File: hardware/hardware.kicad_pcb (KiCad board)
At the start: 2 copper layers, 110.5 x 66.5 mm, 23 parts, among them J1 DIN-5_180degree, U1 Teensy3.2, U2 TeensyAudioShield3.2, U3 6N138

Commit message: Change MIDI Out label to MIDI In
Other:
- board text added: "MIDI In"
- board text removed: "MIDI Out"

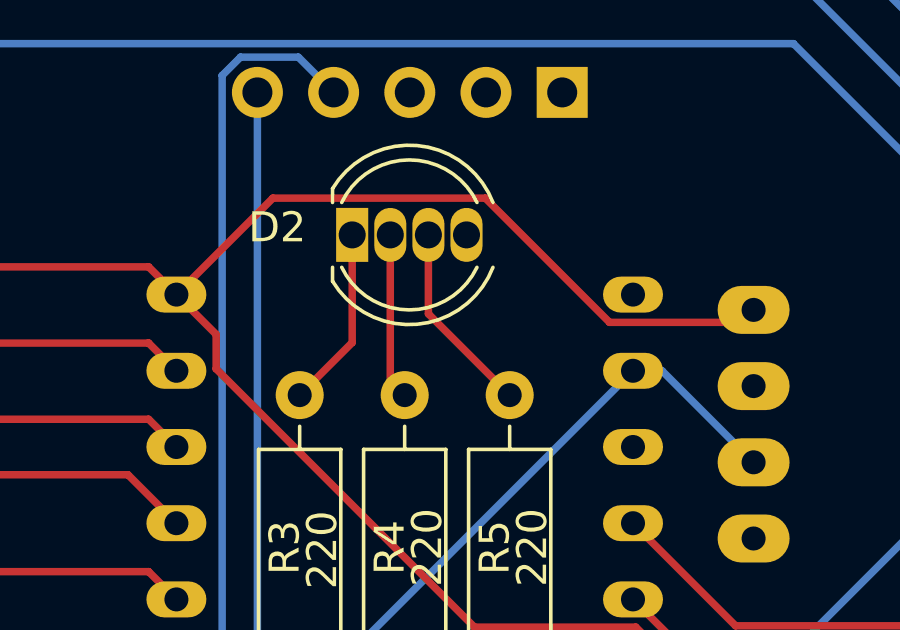
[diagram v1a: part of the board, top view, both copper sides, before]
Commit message: Make footprint match LED pinout even if schematic looks wrong
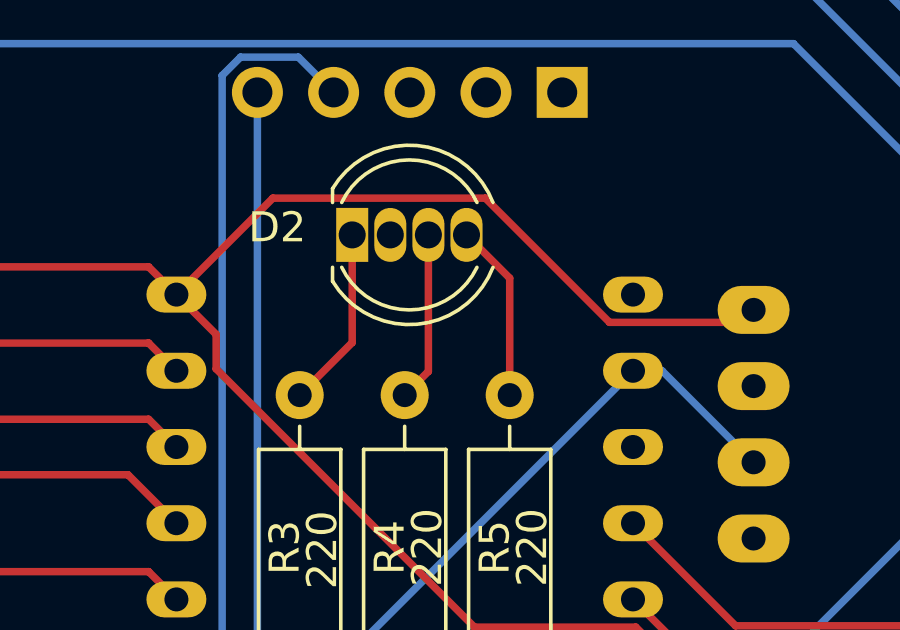
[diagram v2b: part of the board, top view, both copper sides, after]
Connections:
- D2 pad 2: Net-(D2-Pad2) -> GND
- D2 pad 4: GND -> Net-(D2-Pad4)
- J1 pad 1: Net-(J1-Pad1) -> (no net)
- J1 pad 2: Net-(J1-Pad2) -> (no net)
- J1 pad 3: Net-(J1-Pad3) -> (no net)
- R4 pad 2: Net-(D2-Pad2) -> Net-(D2-Pad3)
- R5 pad 2: Net-(D2-Pad3) -> Net-(D2-Pad4)
- TB1 pad 19: Net-(TB1-Pad19) -> (no net)
- TB1 pad 20: Net-(TB1-Pad20) -> (no net)
- TB1 pad 21: Net-(TB1-Pad21) -> (no net)
- TB1 pad 22: Net-(TB1-Pad22) -> (no net)
- TB1 pad 23: Net-(TB1-Pad23) -> (no net)
- TB1 pad 24: Net-(TB1-Pad24) -> (no net)
- U1 pad 19: Net-(U1-Pad19) -> (no net)
- U1 pad 3: Net-(U1-Pad3) -> (no net)
- U2 pad 10: Net-(U2-Pad10) -> (no net)
- U2 pad 18: Net-(U2-Pad18) -> (no net)
- U2 pad 19: Net-(U2-Pad19) -> (no net)
- U2 pad 2: Net-(U2-Pad2) -> (no net)
- U2 pad 22: Net-(U2-Pad22) -> (no net)
- U2 pad 23: Net-(U2-Pad23) -> (no net)
- U2 pad 3: Net-(U2-Pad3) -> (no net)
- U2 pad 4: Net-(U2-Pad4) -> (no net)
- U2 pad 5: Net-(U2-Pad5) -> (no net)
- U2 pad 6: Net-(U2-Pad6) -> (no net)
- U2 pad 7: Net-(U2-Pad7) -> (no net)
- U3 pad 1: Net-(U3-Pad1) -> (no net)
- U3 pad 4: Net-(U3-Pad4) -> (no net)
- U3 pad 7: Net-(U3-Pad7) -> (no net)
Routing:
- net Net-(D2-Pad4): track 0.00 -> 5.94 mm
- net Net-(D2-Pad2): track 5.54 -> 0.00 mm
